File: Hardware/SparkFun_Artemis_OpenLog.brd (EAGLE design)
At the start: 30.5 x 30.5 mm, 122 parts, among them J14 CORTEX_JTAG, J17 MICRO-SD, Q1 20V/0.2A/8MHz/1.2Ω/1Vth, Q10 20V/0.2A/8MHz/1.2Ω/1Vth, Q2 20V/4.2A/52mΩ/1.4W, Q3 20V/0.2A/8MHz/1.2Ω/1Vth, Q4 20V/4.2A/52mΩ/1.4W, Q7 20V/0.2A/8MHz/1.2Ω/1Vth, Q9 20V/0.2A/8MHz/1.2Ω/1Vth, U1 3.0V Supervisor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

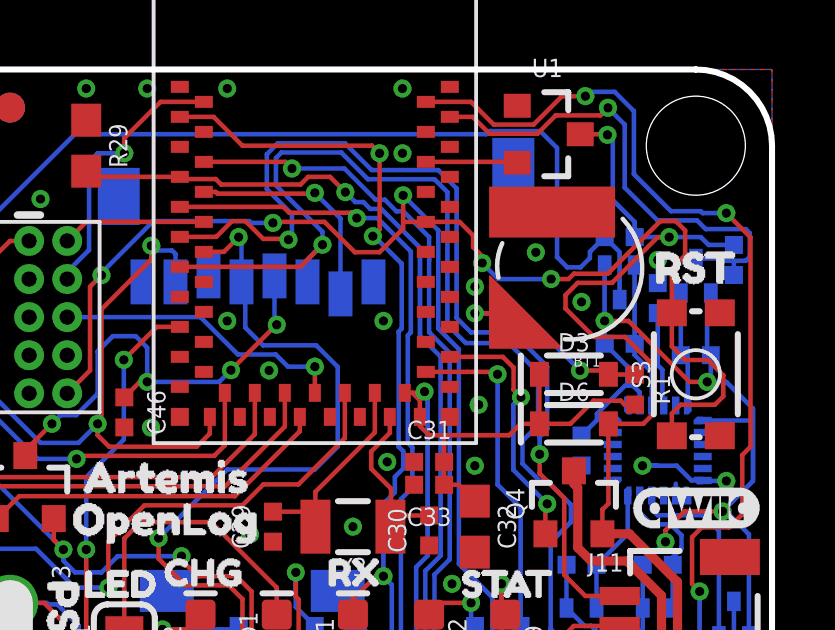
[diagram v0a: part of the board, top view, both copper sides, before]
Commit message: Add dimension and schematic PDFs. Add readme and issue_template.
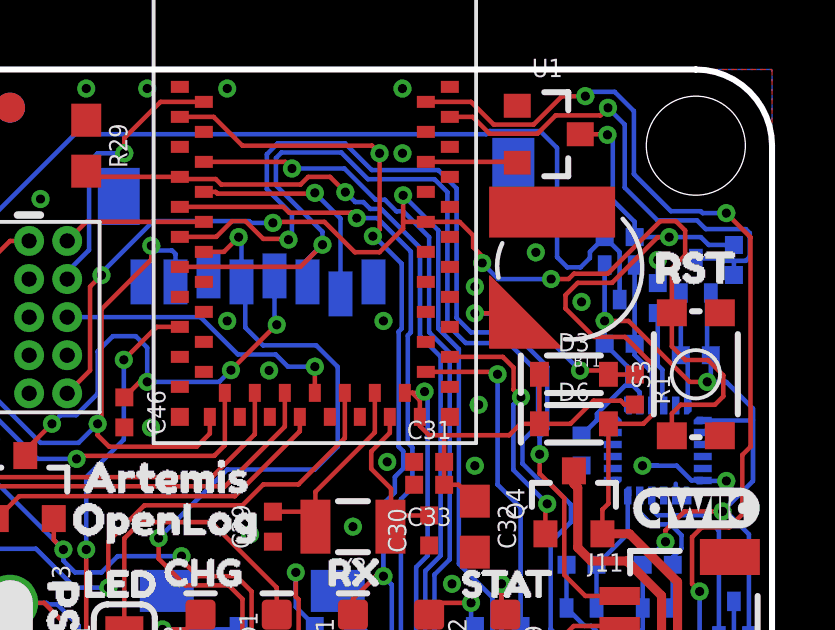
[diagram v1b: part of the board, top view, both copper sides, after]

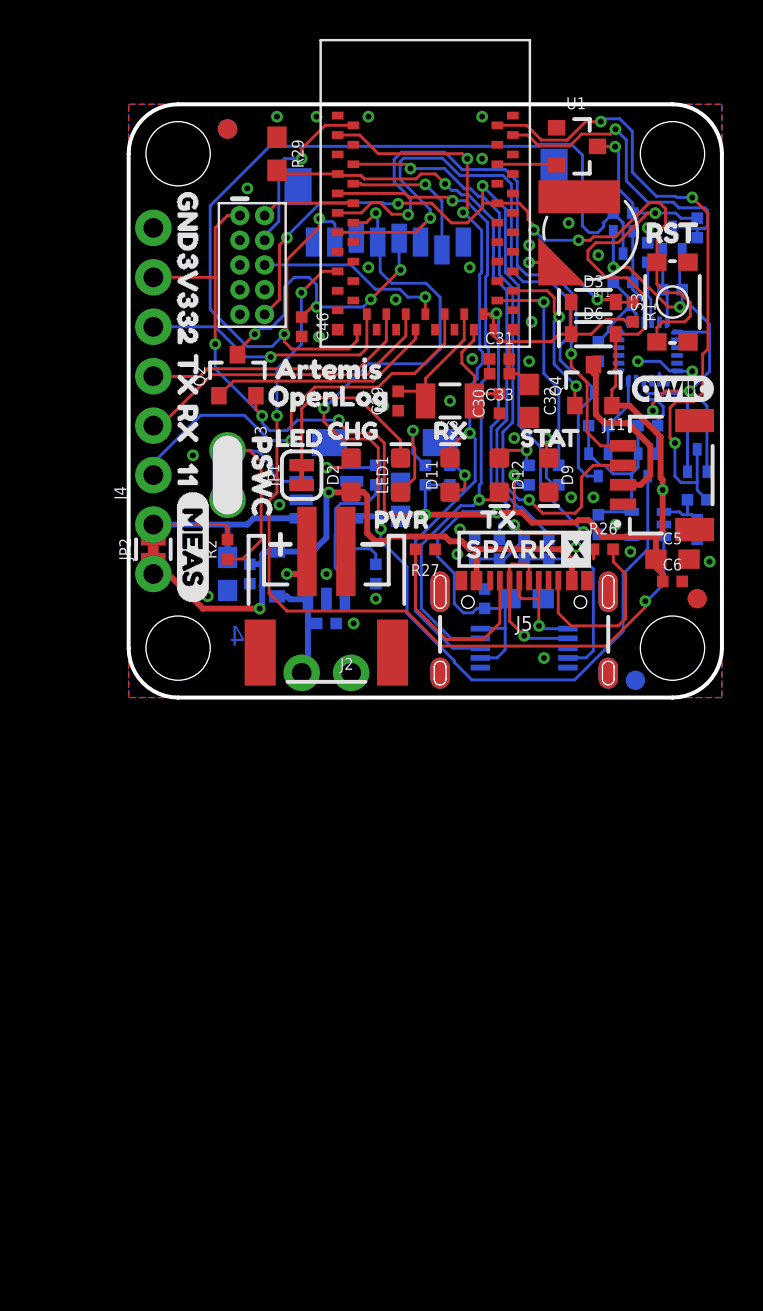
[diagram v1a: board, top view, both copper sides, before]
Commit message: 4 layer PCB, change Qwiic power to vreg, move pwr LED to GPIO, move to SDIO/SPI interface to SD
Changes from x04 to v10:

* ICM_PWR moved from 22 to 27
* SD CS moved from 10 to 23
* PWR_LED is now GPIO 29
* VREG_EN is now 25 through NO jumper
* SD is now SDIO+SPI compatible
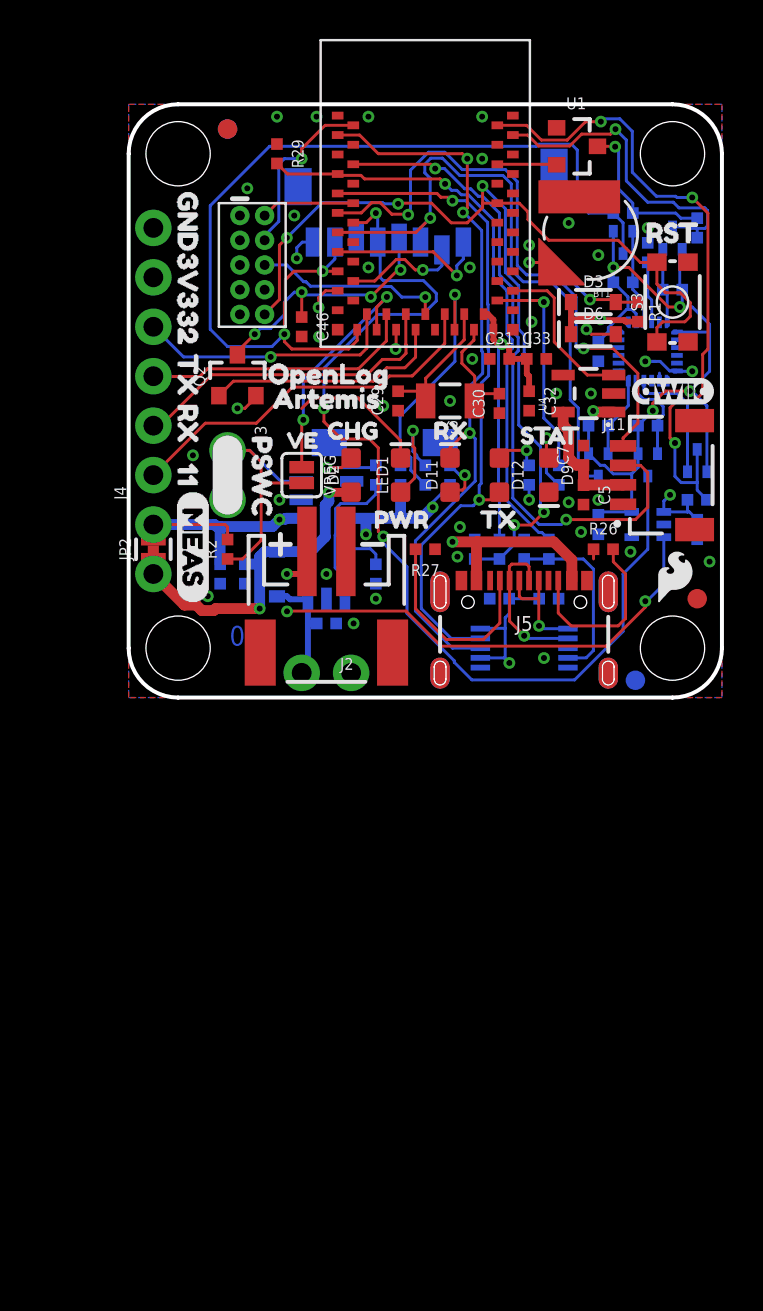
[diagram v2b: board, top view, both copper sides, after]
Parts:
- removed C6: 1.0uF, SparkFun-Capacitors:0402-TIGHT
- removed JP1: (no value), SparkFun-Jumpers:SMT-JUMPER_2_NC_TRACE_SILK
- removed Q4: 20V/4.2A/52mΩ/1.4W, SparkFun-DiscreteSemi:SOT23-3
- removed U$8: (no value), buzzard_labels (15):LED0
- added C7: 2.2uF, SparkFun-Capacitors:0402-TIGHT
- added LOGO1: SFE_LOGO_NAME.1_INCH, SparkFun-Aesthetics:SFE_LOGO_NAME_.1
- added LOGO3: SPECIAL_INSTRUCTIONS-ORDERING, SparkFun-Aesthetics:ORDERING_INSTRUCTIONS
- added LOGO4, LOGO5: SFE_LOGO_FLAME.1_INCH, SparkFun-Aesthetics:SFE_LOGO_FLAME_.1
- added U4: AP2112K, SparkFun-IC-Power:SOT23-5
- added VREG: (no value), SparkFun-Jumpers:SMT-JUMPER_2_NO_SILK
- C1, C2, C32, C40, C5: device SparkFun-Capacitors:0603 -> SparkFun-Capacitors:0402-TIGHT
- R2: value 10k -> 220k
- R29: value 220k -> 220KOHM-0402T-1/16W-1%; device SparkFun-Resistors:0603 -> SparkFun-Resistors:0402-TIGHT
- R49: value 2.2k -> DNP
- U$6: value SPARKX-LOGO3 -> (none); device SparkX:SPARKX-SMALL -> buzzard_labels (19):VE0
- U8: value ARTEMIS_MODULESMD -> ARTEMIS_MODULE
- moved U$6 14.1 mm to (7.37, 13.2)
- moved C5 5.64 mm to (23.4, 10.4), turned to 270 degrees
- moved C33 2.05 mm to (21.0, 17.4), turned to 0 degrees
- moved U$9 1.53 mm to (6.48, 15.4)
- moved C2 1.27 mm to (14.0, 11.4)
- moved C40 1.14 mm to (21.6, 5.08)
- moved U$28 1.14 mm to (6.22, 16.6)
- moved C41 0.76 mm to (19.1, 5.08), turned to 0 degrees
- moved C1 0.38 mm to (4.70, 6.35)
- moved C3 0.25 mm to (5.97, 6.35)
- moved R1 0.25 mm to (26.2, 19.8)
- moved U$1 0.13 mm to (27.9, 15.7)
- moved U$5 0.13 mm to (19.3, 13.5)
- renumbered J17 to J6
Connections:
- net ARTEMIS_D33 renamed SWO
- net MOSI renamed MOSI/SDIO-CMD
- net SCK renamed SCK/SDIO-CLK
- removed net ARTEMIS_D16: U8.AD16
- removed net ARTEMIS_D29: U8.~AD29
- removed net ARTEMIS_D31: U8.~AD31
- removed net ARTEMIS_D34: U8.AD34
- removed net ARTEMIS_D35: U8.~AD35
- removed net MICROSD_!CS!: J6.CS, U8.D10
- removed net MISO: J6.DO, Q10.3, R49.1, U8.~D6
- removed net N$4: JP1.2, LED1.C
- removed net N$5: J11.2, Q4.3
- new net MICROSD_!CS!/SDIO3: J6.CS, U8.~D23
- new net MISO/SDIO0: J6.DO, Q10.3, R49.1, U8.~D22, U8.~D6
- new net PWR_LED: R22.2, U8.~AD29
- new net QWIIC_3.3V: C5.1, C7.1, J11.2, U4.5
- new net SDIO1: J6.RSV2, U8.~D26
- new net SDIO2: J6.RSV1, U8.~D4
- new net VREG_EN1: U8.~D25, VREG.1
- net 3.3V: no longer C5.1, C6.1, Q4.2, R22.2
- net GND: now also C7.2, J6.GND1, J6.GND3, LED1.C, U4.2; no longer C6.2, JP1.1
- net ICM_PWR: now also U8.~D27; no longer U8.~D22
- net QWIIC_PWR: now also U4.3; no longer Q4.1
- net VIN: now also U4.1
- net VREG_EN: now also VREG.2
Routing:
- net 3.3V: track 106.8 -> 31.5 mm, vias 9 -> 8
- net MISO: track 52.6 -> 0.00 mm, vias 2 -> 0
- net MISO/SDIO0: track 0.00 -> 50.6 mm, vias 0 -> 2
- net VIN: track 14.7 -> 34.6 mm, vias 0 -> 2
- net PWR_LED: track 0.00 -> 13.5 mm, vias 0 -> 1
- net VREG_EN1: track 0.00 -> 12.5 mm, vias 0 -> 2
- net N$4: track 10.0 -> 0.00 mm
- net SDIO1: track 0.00 -> 9.81 mm, vias 0 -> 2
- net N$5: track 9.18 -> 0.00 mm
- net SDIO2: track 0.00 -> 8.48 mm, vias 0 -> 1
- net ARTEMIS_!RESET: track 65.8 -> 58.2 mm, vias 7 -> 5
- net MICROSD_!CS!: track 7.47 -> 0.00 mm, vias 1 -> 0
- net GND: track 5.17 -> 11.9 mm, vias 37 -> 36
- net QWIIC_3.3V: track 0.00 -> 6.46 mm
- net MICROSD_!CS!/SDIO3: track 0.00 -> 6.13 mm, vias 0 -> 1
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- added copper zone on layer 15, net 3.3V
- added copper zone on layer 2, net GND
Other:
- board text added: "1.6mm thickness"
- board text added: "4-layer board"
- board text added: "ENIG finish"
- board text added: "v10"
- board text removed: "x04"

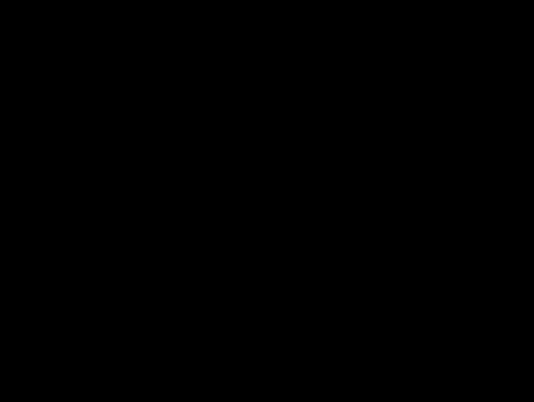
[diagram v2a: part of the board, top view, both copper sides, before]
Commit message: Add pull down to Qwiic vreg
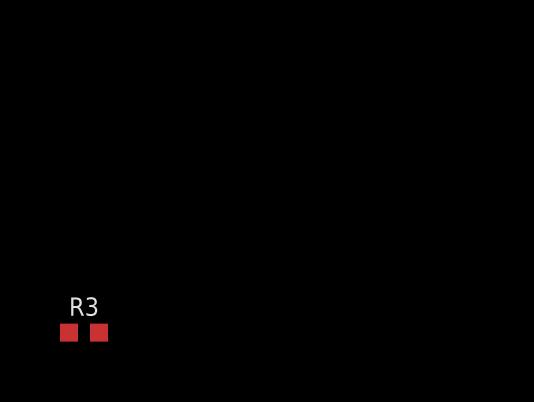
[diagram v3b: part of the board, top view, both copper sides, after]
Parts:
- added R3: 220k, SparkFun-Resistors:0402-TIGHT
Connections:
- net GND: now also R3.1
- net QWIIC_PWR: now also R3.2
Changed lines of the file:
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@@
 <element name="LOGO1" library="SparkFun-Aesthetics" package="SFE_LOGO_NAME_.1" value="SFE_LOGO_NAME.1_INCH" x="15.24" y="28.829" smashed="yes" rot="MR0"/>
 <element name="LOGO5" library="SparkFun-Aesthetics" package="SFE_LOGO_FLAME_.1" value="SFE_LOGO_FLAME.1_INCH" x="15.113" y="3.556" smashed="yes" rot="MR0"/>
+<element name="R3" library="SparkFun-Resistors" package="0402-TIGHT" value="220k" x="-3.81" y="-29.21" smashed="yes">
+<attribute name="NAME" x="-3.81" y="-28.648" size="0.6096" layer="25" font="vector" ratio="20" align="bottom-center"/>
+<attribute name="PROD_ID" value="RES-15094" x="-3.81" y="-29.21" size="1.778" layer="27" font="vector" ratio="15" display="off"/>
+<attribute name="VALUE" x="-3.81" y="-29.772" size="0.6096" layer="27" font="vector" ratio="20" align="top-center"/>
+</element>
 </elements>
 <signals>
@@
 <contactref element="U4" pad="2"/>
 <via x="23.749" y="15.621" extent="1-16" drill="0.3048"/>
+<contactref element="R3" pad="1"/>
+<wire x1="26.67" y1="23.36" x2="28.74" y2="22.37" width="0" layer="19" extent="1-16"/>
+<wire x1="24.13" y1="22.733" x2="26.67" y2="23.36" width="0" layer="19" extent="16-16"/>
+<wire x1="22.606" y1="24.384" x2="24.13" y2="22.733" width="0" layer="19" extent="1-1"/>
+<wire x1="23.149" y1="25.726" x2="22.606" y2="24.384" width="0" layer="19" extent="1-1"/>
+<wire x1="21.855" y1="27.25" x2="23.149" y2="25.726" width="0" layer="19" extent="1-16"/>
+<wire x1="21.987" y1="29.271" x2="21.855" y2="27.25" width="0" layer="19" extent="1-16"/>
+<wire x1="19.74" y1="29.9" x2="21.987" y2="29.271" width="0" layer="19" extent="1-1"/>
+<wire x1="18.161" y1="29.845" x2="19.74" y2="29.9" width="0" layer="19" extent="1-1"/>
+<wire x1="18.161" y1="27.686" x2="18.161" y2="29.845" width="0" layer="19" extent="1-1"/>
+<wire x1="20.574" y1="23.241" x2="22.606" y2="24.384" width="0" layer="19" extent="1-1"/>
+<wire x1="19.74" y1="23.9" x2="20.574" y2="23.241" width="0" layer="19" extent="1-1"/>
+<wire x1="17.526" y1="22.098" x2="19.74" y2="23.9" width="0" layer="19" extent="1-1"/>
+<wire x1="19.74" y1="19.9" x2="17.526" y2="22.098" width="0" layer="19" extent="1-1"/>
+<wire x1="19.74" y1="18.9" x2="19.74" y2="19.9" width="0" layer="19" extent="1-1"/>
+<wire x1="20.701" y1="19.304" x2="19.74" y2="18.9" width="0" layer="19" extent="1-1"/>
+<wire x1="18.55" y1="17.399" x2="19.74" y2="18.9" width="0" layer="19" extent="1-1"/>
+<wire x1="17.653" y1="17.399" x2="18.55" y2="17.399" width="0" layer="19" extent="1-1"/>
+<wire x1="21.455" y1="17.399" x2="20.701" y2="19.304" width="0" layer="19" extent="1-1"/>
+<wire x1="21.971" y1="15.621" x2="21.455" y2="17.399" width="0" layer="19" extent="1-1"/>
+<wire x1="20.574" y1="14.74" x2="21.971" y2="15.621" width="0" layer="19" extent="1-1"/>
+<wire x1="19.05" y1="14.613" x2="20.574" y2="14.74" width="0" layer="19" extent="1-1"/>
+<wire x1="23.749" y1="15.621" x2="21.971" y2="15.621" width="0" layer="19" extent="1-1"/>
+<wire x1="24.9221" y1="15.621" x2="23.749" y2="15.621" width="0" layer="19" extent="1-1"/>
+<wire x1="24.13" y1="17.28" x2="23.749" y2="15.621" width="0" layer="19" extent="16-16"/>
+<wire x1="26.543" y1="17.272" x2="24.9221" y2="15.621" width="0" layer="19" extent="1-1"/>
+<wire x1="27.27" y1="16.672" x2="27.051" y2="17.272" width="0" layer="19" extent="16-16"/>
+<wire x1="28.74" y1="18.27" x2="28.956" y2="16.764" width="0" layer="19" extent="1-1"/>
+<wire x1="16.51" y1="15.24" x2="17.653" y2="17.399" width="0" layer="19" extent="1-1"/>
+<wire x1="23.368" y1="12.946" x2="23.749" y2="15.621" width="0" layer="19" extent="1-1"/>
+<wire x1="13.843" y1="14.74" x2="16.51" y2="15.24" width="0" layer="19" extent="1-1"/>
+<wire x1="13.081" y1="14.986" x2="13.843" y2="14.74" width="0" layer="19" extent="1-1"/>
+<wire x1="13.97" y1="12.307" x2="13.843" y2="14.74" width="0" layer="19" extent="1-1"/>
+<wire x1="13.97" y1="11.93" x2="13.97" y2="12.307" width="0" layer="19" extent="1-16"/>
+<wire x1="10.305" y1="13.1" x2="8.89" y2="14.85134375" width="0" layer="19" extent="1-16"/>
+<wire x1="24.13" y1="10.16" x2="23.368" y2="12.946" width="0" layer="19" extent="1-1"/>
+<wire x1="23.368" y1="9.914" x2="24.13" y2="10.16" width="0" layer="19" extent="1-1"/>
+<wire x1="22.606" y1="10.033" x2="23.368" y2="9.914" width="0" layer="19" extent="1-1"/>
+<wire x1="21.59" y1="10.553" x2="22.606" y2="10.033" width="0" layer="19" extent="1-1"/>
+<wire x1="25.4" y1="9.93" x2="24.13" y2="10.16" width="0" layer="19" extent="1-1"/>
+<wire x1="23.241" y1="8.509" x2="23.368" y2="9.914" width="0" layer="19" extent="1-1"/>
+<wire x1="24.13" y1="8.39" x2="23.241" y2="8.509" width="0" layer="19" extent="16-16"/>
+<wire x1="23.884" y1="7.62" x2="24.13" y2="8.39" width="0" layer="19" extent="1-16"/>
+<wire x1="23.545" y1="6.01" x2="23.884" y2="7.12" width="0" layer="19" extent="1-1"/>
+<wire x1="22.09" y1="5.08" x2="23.545" y2="6.01" width="0" layer="19" extent="1-16"/>
+<wire x1="25.781" y1="7.493" x2="24.13" y2="8.39" width="0" layer="19" extent="16-16"/>
+<wire x1="27.495" y1="8.89" x2="25.781" y2="7.493" width="0" layer="19" extent="16-16"/>
+<wire x1="29.21" y1="8.136" x2="27.495" y2="8.89" width="0" layer="19" extent="16-16"/>
+<wire x1="29.845" y1="6.985" x2="29.21" y2="8.136" width="0" layer="19" extent="16-16"/>
+<wire x1="22.57" y1="2.54" x2="22.09" y2="5.08" width="0" layer="19" extent="16-16"/>
+<wire x1="21.336" y1="2.032" x2="22.57" y2="2.54" width="0" layer="19" extent="16-16"/>
+<wire x1="8.8599" y1="10.16" x2="10.305" y2="13.1" width="0" layer="19" extent="16-16"/>
+<wire x1="7.747" y1="10.16" x2="8.8599" y2="10.16" width="0" layer="19" extent="16-16"/>
+<wire x1="5.08" y1="10.16" x2="7.747" y2="10.16" width="0" layer="19" extent="1-1"/>
+<wire x1="3.302" y1="12.446" x2="5.08" y2="10.16" width="0" layer="19" extent="1-1"/>
+<wire x1="11.16" y1="7.51" x2="8.8599" y2="10.16" width="0" layer="19" extent="1-16"/>
+<wire x1="10.16" y1="6.35" x2="11.16" y2="7.51" width="0" layer="19" extent="1-1"/>
+<wire x1="10.16" y1="5.0499" x2="10.16" y2="6.35" width="0" layer="19" extent="16-16"/>
+<wire x1="10.66" y1="3.81" x2="10.16" y2="5.0499" width="0" layer="19" extent="16-16"/>
+<wire x1="11.557" y1="3.81" x2="10.66" y2="3.81" width="0" layer="19" extent="16-16"/>
+<wire x1="12.7" y1="5.08" x2="11.557" y2="3.81" width="0" layer="19" extent="1-1"/>
+<wire x1="12.7" y1="5.85" x2="12.7" y2="5.08" width="0" layer="19" extent="16-16"/>
+<wire x1="11.43" y1="1.27" x2="11.557" y2="3.81" width="0" layer="19" extent="1-1"/>
+<wire x1="15.74" y1="7.62" x2="12.7" y2="5.85" width="0" layer="19" extent="1-16"/>
+<wire x1="16.891" y1="7.239" x2="15.74" y2="7.62" width="0" layer="19" extent="1-1"/>
+<wire x1="17.78" y1="8.12" x2="16.891" y2="7.239" width="0" layer="19" extent="16-16"/>
+<wire x1="17.018" y1="8.763" x2="17.78" y2="8.12" width="0" layer="19" extent="16-16"/>
+<wire x1="17.095" y1="6.01" x2="16.891" y2="7.239" width="0" layer="19" extent="1-1"/>
+<wire x1="18.55" y1="5.08" x2="17.095" y2="6.01" width="0" layer="19" extent="1-16"/>
+<wire x1="8.89" y1="18.55" x2="8.89" y2="14.85134375" width="0" layer="19" extent="1-1"/>
+<wire x1="9.779" y1="18.542" x2="8.89" y2="18.55" width="0" layer="19" extent="1-1"/>
+<wire x1="10.74" y1="18.9" x2="9.779" y2="18.542" width="0" layer="19" extent="1-1"/>
+<wire x1="5.715" y1="19.685" x2="8.89" y2="18.55" width="0" layer="19" extent="1-1"/>
+<wire x1="5.715" y1="22.225" x2="5.715" y2="19.685" width="0" layer="19" extent="1-1"/>
+<wire x1="5.715" y1="23.495" x2="5.715" y2="22.225" width="0" layer="19" extent="1-1"/>
+<wire x1="6.096" y1="26.162" x2="5.715" y2="23.495" width="0" layer="19" extent="1-1"/>
+<wire x1="8.705" y1="26.25" x2="6.096" y2="26.162" width="0" layer="19" extent="16-16"/>
+<wire x1="8.509" y1="24.765" x2="8.705" y2="26.25" width="0" layer="19" extent="16-16"/>
+<wire x1="7.62" y1="28.44" x2="8.705" y2="26.25" width="0" layer="19" extent="1-16"/>
+<wire x1="7.62" y1="29.845" x2="7.62" y2="28.44" width="0" layer="19" extent="1-1"/>
+<wire x1="9.652" y1="29.845" x2="7.62" y2="29.845" width="0" layer="19" extent="1-1"/>
+<wire x1="10.74" y1="29.9" x2="9.652" y2="29.845" width="0" layer="19" extent="1-1"/>
+<wire x1="12.319" y1="29.845" x2="10.74" y2="29.9" width="0" layer="19" extent="1-1"/>
+<wire x1="11.695" y1="23.6" x2="8.509" y2="24.765" width="0" layer="19" extent="16-16"/>
+<wire x1="12.319" y1="22.098" x2="11.695" y2="23.6" width="0" layer="19" extent="16-16"/>
+<wire x1="5.969" y1="5.85" x2="10.16" y2="6.35" width="0" layer="19" extent="16-16"/>
+<wire x1="4.699" y1="5.85" x2="5.969" y2="5.85" width="0" layer="19" extent="16-16"/>
+<wire x1="4.064" y1="5.207" x2="4.699" y2="5.85" width="0" layer="19" extent="16-16"/>
+<wire x1="1.27" y1="24.13" x2="5.715" y2="23.495" width="0" layer="19" extent="1-1"/>
+<wire x1="-4.31" y1="-29.21" x2="11.43" y2="1.27" width="0" layer="19" extent="1-1"/>
 </signal>
 <signal name="3.3V">
@@
 <wire x1="24.9221" y1="16.571" x2="23.561" y2="16.571" width="0.1524" layer="1"/>
 <wire x1="23.561" y1="16.571" x2="21.86405625" y2="18.26794375" width="0.1524" layer="1"/>
+<contactref element="R3" pad="2"/>
+<wire x1="-3.31" y1="-29.21" x2="24.9221" y2="16.571" width="0" layer="19" extent="1-1"/>
 </signal>
 <signal name="SD_PWR">
